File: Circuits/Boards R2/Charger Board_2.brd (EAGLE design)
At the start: 101.6 x 69.8 mm, 100 parts, among them CON1 ISP(2X3), CON10 HEADER_3X1, CON11 HEADER_3X1, CON12 HEADER_3X1, CON13 HEADER_4X1, CON14 HEADER_3X1, CON15 HEADER_3X1, CON16 HEADER_4X1, CON17 HEADER_3X1, CON18 HEADER_3X1, CON2 SCREWTERMINAL_1X2, CON3 HEADER_3X1, CON4 HEADER_3X1, CON5 HEADER_3X1, CON6 HEADER_3X1, CON7 HEADER_3X1, CON8 HEADER_3X1, CON9 HEADER_3X1, IC1 NCP1117DT33G, T1 NPN2N2222, T2 NPN2N2222, T3 SI4421DY, T4 MMSS8550-L, T5 MMSS8550-L, T6 MMSS8550-L, U1 ATMEGA324P, U2 ACS711, U3 JOYSTICKPTH, U4 MX25L25735E

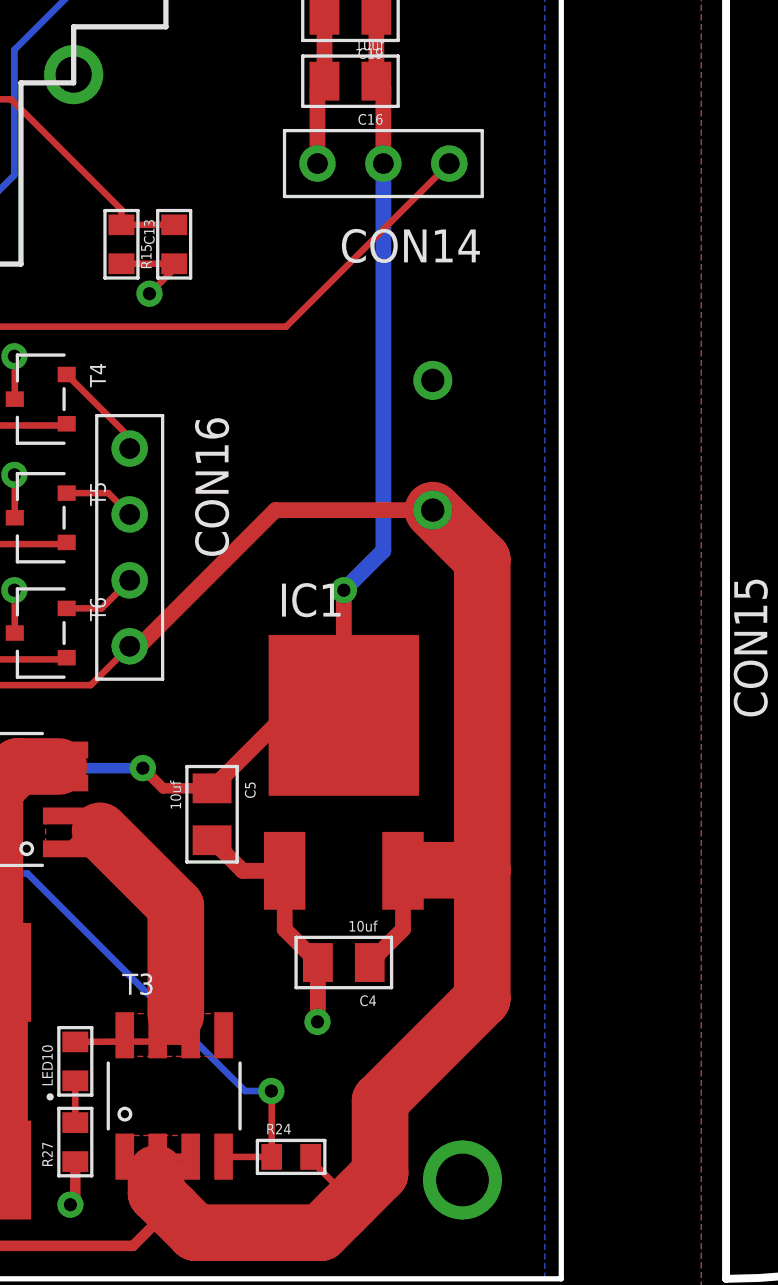
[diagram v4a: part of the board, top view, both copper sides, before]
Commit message: slight updates to part values to account for availibility
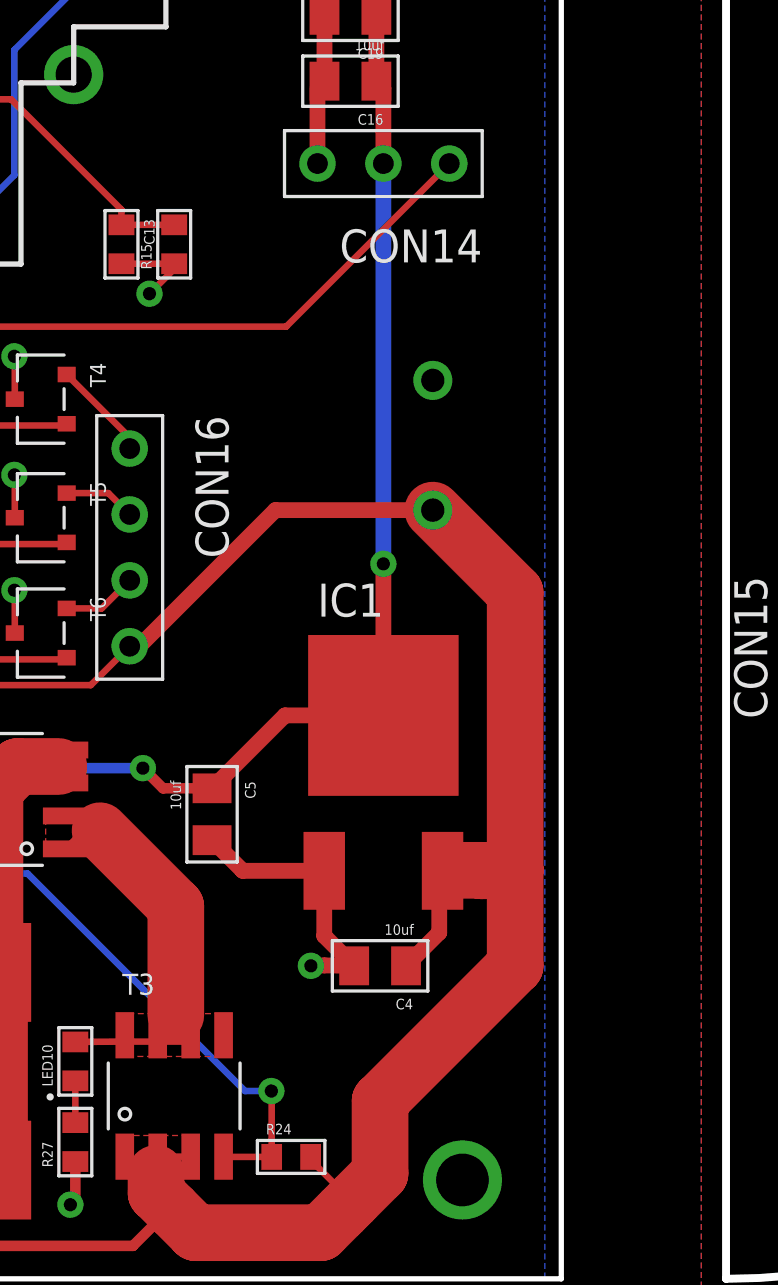
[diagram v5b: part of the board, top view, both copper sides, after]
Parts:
- R10, R11, R12, R13, R14, R25: value 18 -> 15
- moved IC1 1.52 mm to (63.0, 21.7)
- moved C4 1.40 mm to (62.9, 12.1)
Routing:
- net +5V: track 116.1 -> 117.1 mm
- net GND: track 70.6 -> 71.6 mm
- net +3V3: track 229.9 -> 230.8 mm
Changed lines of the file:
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@@
 <?xml version="1.0" encoding="utf-8"?>
 <!DOCTYPE eagle SYSTEM "eagle.dtd">
-<eagle version="6.3">
+<eagle version="6.2">
 <drawing>
 <settings>
@@
 </class>
 </classes>
-<designrules name="default">
+<designrules>
 <description language="en">&lt;b&gt;EAGLE Design Rules&lt;/b&gt;
 &lt;p&gt;
@@
 <element name="T1" library="Passive" package="SOT23" value="NPN2N2222" x="26.2255" y="54.6735" rot="R180"/>
 <element name="T2" library="Passive" package="SOT23" value="NPN2N2222" x="87.9475" y="21.9075" rot="R90"/>
-<element name="R10" library="Passive" package="0603" value="18" x="94.2975" y="15.5575" rot="R180"/>
-<element name="R11" library="Passive" package="0603" value="18" x="79.6925" y="10.795" rot="R270"/>
-<element name="R12" library="Passive" package="0603" value="18" x="93.345" y="35.8775" rot="R180"/>
-<element name="R13" library="Passive" package="0603" value="18" x="86.0425" y="43.4975" rot="R270"/>
-<element name="R14" library="Passive" package="0603" value="18" x="96.2025" y="26.67" rot="R180"/>
+<element name="R10" library="Passive" package="0603" value="15" x="94.2975" y="15.5575" rot="R180"/>
+<element name="R11" library="Passive" package="0603" value="15" x="79.6925" y="10.795" rot="R270"/>
+<element name="R12" library="Passive" package="0603" value="15" x="93.345" y="35.8775" rot="R180"/>
+<element name="R13" library="Passive" package="0603" value="15" x="86.0425" y="43.4975" rot="R270"/>
+<element name="R14" library="Passive" package="0603" value="15" x="96.2025" y="26.67" rot="R180"/>
 <element name="R16" library="Passive" package="0603" value="1k" x="83.82" y="22.86"/>
 <element name="LED2" library="Passive" package="5MM_LED_RA" value="IR" x="93.726" y="20.447" rot="R255"/>
@@
 <element name="CON11" library="Mechanical" package="3PINHEADER_.100&quot;" value="HEADER_3X1" x="34.29" y="8.001" rot="R90"/>
 <element name="CON12" library="Mechanical" package="3PINHEADER_.100&quot;" value="HEADER_3X1" x="36.83" y="8.001" rot="R90"/>
-<element name="IC1" library="PowerIC" package="DPAK" value="NCP1117DT33G" x="61.468" y="21.717"/>
-<element name="C4" library="Passive" package="0805" value="10uf" x="61.468" y="12.192" rot="R180"/>
+<element name="IC1" library="PowerIC" package="DPAK" value="NCP1117DT33G" x="62.992" y="21.717"/>
+<element name="C4" library="Passive" package="0805" value="10uf" x="62.865" y="12.065" rot="R180"/>
 <element name="C5" library="Passive" package="0805" value="10uf" x="56.388" y="17.907" rot="R270"/>
 <element name="T3" library="Passive" package="S0-8" value="SI4421DY" x="54.9275" y="7.0485"/>
@@
 <element name="C21" library="Passive" package="0603" value=".1uf" x="61.722" y="54.737" rot="R180"/>
 <element name="LED7" library="Passive" package="5MM_LED_RA" value="IR" x="89.66835" y="11.93165" rot="R225"/>
-<element name="R25" library="Passive" package="0603" value="18" x="86.36" y="8.5725" rot="R90"/>
+<element name="R25" library="Passive" package="0603" value="15" x="86.36" y="8.5725" rot="R90"/>
 <element name="H5" library="Mechanical" package="MOUNTINGHOLE" value="MOUNTINGHOLE" x="80.01" y="35.56"/>
 <element name="H6" library="Mechanical" package="MOUNTINGHOLE" value="MOUNTINGHOLE" x="80.01" y="15.24"/>
@@
 <vertex x="0" y="0"/>
 </polygon>
-<wire x1="59.188" y1="15.727" x2="57.568" y2="15.727" width="0.6096" layer="1"/>
+<wire x1="60.712" y1="15.727" x2="57.568" y2="15.727" width="0.6096" layer="1"/>
 <wire x1="57.568" y1="15.727" x2="56.388" y2="16.907" width="0.6096" layer="1"/>
-<wire x1="59.188" y1="15.727" x2="59.188" y2="13.472" width="0.6096" layer="1"/>
-<wire x1="59.188" y1="13.472" x2="60.468" y2="12.192" width="0.6096" layer="1"/>
+<wire x1="60.712" y1="15.727" x2="60.712" y2="13.218" width="0.6096" layer="1"/>
+<wire x1="60.712" y1="13.218" x2="61.865" y2="12.065" width="0.6096" layer="1"/>
 <wire x1="3.556" y1="20.816" x2="3.556" y2="22.364" width="0.254" layer="1"/>
 <wire x1="3.556" y1="20.816" x2="2.802" y2="20.82" width="0.254" layer="1"/>
@@
 <wire x1="24.13" y1="28.575" x2="23.876" y2="28.321" width="0.254" layer="1"/>
 <via x="23.876" y="28.321" extent="1-16" drill="0.508"/>
-<wire x1="60.468" y1="12.192" x2="60.468" y2="9.922" width="0.6096" layer="1"/>
-<wire x1="60.468" y1="9.922" x2="60.452" y2="9.906" width="0.6096" layer="1"/>
-<via x="60.452" y="9.906" extent="1-16" drill="0.508"/>
+<wire x1="61.865" y1="12.065" x2="60.722" y2="12.081" width="0.6096" layer="1"/>
+<wire x1="60.722" y1="12.081" x2="60.198" y2="12.065" width="0.6096" layer="1"/>
+<via x="60.198" y="12.065" extent="1-16" drill="0.508"/>
 <wire x1="18.38" y1="25.4" x2="16.891" y2="25.4" width="0.254" layer="1"/>
 <wire x1="16.891" y1="25.4" x2="16.764" y2="25.273" width="0.254" layer="1"/>
@@
 <contactref element="IC1" pad="3"/>
 <contactref element="C4" pad="1"/>
-<wire x1="63.748" y1="15.727" x2="63.748" y2="15.24" width="0.6096" layer="1"/>
-<wire x1="63.748" y1="15.24" x2="63.748" y2="13.472" width="0.6096" layer="1"/>
-<wire x1="63.748" y1="13.472" x2="62.468" y2="12.192" width="0.6096" layer="1"/>
+<wire x1="65.272" y1="15.727" x2="65.145" y2="15.24" width="0.6096" layer="1"/>
+<wire x1="65.145" y1="15.24" x2="65.145" y2="13.345" width="0.6096" layer="1"/>
+<wire x1="65.145" y1="13.345" x2="63.865" y2="12.065" width="0.6096" layer="1"/>
 <polygon width="0.254" layer="1" thermals="no">
 <vertex x="55.8165" y="3.8735"/>
@@
 <contactref element="LED1" pad="2"/>
 <contactref element="CON13" pad="1"/>
-<wire x1="66.781" y1="15.727" x2="66.802" y2="15.748" width="2.1844" layer="1"/>
+<wire x1="66.781" y1="15.727" x2="68.072" y2="15.748" width="2.1844" layer="1"/>
 <wire x1="61.4045" y1="2.6035" x2="60.579" y2="1.778" width="2.1844" layer="1"/>
 <wire x1="60.579" y1="1.778" x2="55.753" y2="1.778" width="2.1844" layer="1"/>
@@
 <wire x1="53.975" y1="4.391" x2="53.975" y2="4.191" width="0.254" layer="1"/>
 <wire x1="61.4045" y1="3.4805" x2="61.4045" y2="2.6035" width="0.254" layer="1"/>
-<wire x1="66.802" y1="15.748" x2="66.802" y2="10.795" width="2.1844" layer="1"/>
-<wire x1="66.802" y1="10.795" x2="62.865" y2="6.858" width="2.1844" layer="1"/>
+<wire x1="68.072" y1="15.748" x2="68.072" y2="12.065" width="2.1844" layer="1"/>
+<wire x1="68.072" y1="12.065" x2="62.865" y2="6.858" width="2.1844" layer="1"/>
 <wire x1="62.865" y1="6.858" x2="62.865" y2="4.064" width="2.1844" layer="1"/>
 <wire x1="62.865" y1="4.064" x2="61.7855" y2="2.9845" width="2.1844" layer="1"/>
 <wire x1="61.7855" y1="2.9845" x2="61.4045" y2="2.6035" width="2.1844" layer="1"/>
-<wire x1="64.897" y1="29.631" x2="66.802" y2="27.726" width="2.1844" layer="1"/>
-<wire x1="66.802" y1="27.726" x2="66.802" y2="15.748" width="2.1844" layer="1"/>
+<wire x1="64.897" y1="29.631" x2="68.072" y2="26.456" width="2.1844" layer="1"/>
+<wire x1="68.072" y1="26.456" x2="68.072" y2="15.748" width="2.1844" layer="1"/>
 <wire x1="66.781" y1="15.727" x2="66.76" y2="15.748" width="2.1844" layer="1"/>
-<wire x1="66.76" y1="15.748" x2="64.389" y2="15.748" width="2.1844" layer="1"/>
-<wire x1="64.389" y1="15.748" x2="63.881" y2="15.24" width="0.2032" layer="1"/>
-<wire x1="63.881" y1="15.24" x2="63.748" y2="15.24" width="0.2032" layer="1"/>
+<wire x1="66.76" y1="15.748" x2="65.913" y2="15.748" width="2.1844" layer="1"/>
+<wire x1="65.913" y1="15.748" x2="65.532" y2="15.367" width="0.2032" layer="1"/>
+<wire x1="65.532" y1="15.367" x2="65.145" y2="15.24" width="0.2032" layer="1"/>
 <contactref element="R24" pad="2"/>
 <contactref element="CON16" pad="4"/>
@@
 <contactref element="C5" pad="1"/>
 <wire x1="56.388" y1="18.907" x2="59.198" y2="21.717" width="0.6096" layer="1"/>
-<wire x1="59.198" y1="21.717" x2="61.468" y2="21.717" width="0.6096" layer="1"/>
+<wire x1="59.198" y1="21.717" x2="62.992" y2="21.717" width="0.6096" layer="1"/>
 <wire x1="18.38" y1="26.2" x2="24.13" y2="26.2" width="0.254" layer="1"/>
 <wire x1="24.13" y1="26.2" x2="27.051" y2="26.2" width="0.254" layer="1"/>
@@
 <wire x1="46.609" y1="40.386" x2="46.482" y2="40.259" width="0.254" layer="16"/>
 <wire x1="46.482" y1="40.259" x2="46.482" y2="19.685" width="0.254" layer="16"/>
-<wire x1="62.992" y1="42.9895" x2="62.992" y2="28.067" width="0.6096" layer="16"/>
-<wire x1="62.992" y1="28.067" x2="61.468" y2="26.543" width="0.6096" layer="16"/>
-<via x="61.468" y="26.543" extent="1-16" drill="0.508"/>
-<wire x1="61.468" y1="26.543" x2="61.468" y2="21.717" width="0.6096" layer="1"/>
+<wire x1="62.992" y1="42.9895" x2="62.992" y2="27.559" width="0.6096" layer="16"/>
+<via x="62.992" y="27.559" extent="1-16" drill="0.508"/>
+<wire x1="62.992" y1="27.559" x2="62.992" y2="21.717" width="0.6096" layer="1"/>
 <wire x1="62.992" y1="42.9895" x2="62.992" y2="45.8945" width="0.6096" layer="1"/>
 <wire x1="62.992" y1="45.8945" x2="62.722" y2="46.1645" width="0.6096" layer="1"/>

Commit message: added gerbers for production
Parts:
- moved CON15 4.45 mm to (75.9, 25.4)
- moved H5 4.45 mm to (75.6, 35.6)
- moved H6 4.45 mm to (75.6, 15.2)
- moved LED3 4.45 mm to (76.7, 7.87)
- moved LED4 4.45 mm to (85.2, 38.9)
- moved LED7 4.45 mm to (85.2, 11.9)
- moved R13 4.45 mm to (81.6, 43.5)
- moved R14 4.45 mm to (91.8, 26.7)
- moved T2 4.45 mm to (83.5, 21.9)
- moved C12 4.44 mm to (81.3, 27.0)
- moved C2 4.44 mm to (83.2, 27.0)
- moved C6 4.44 mm to (80.3, 31.1)
- moved C7 4.44 mm to (85.1, 27.0)
- moved C8 4.44 mm to (80.3, 33.7)
- moved C9 4.44 mm to (79.4, 27.0)
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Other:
- board size 101.6 x 69.8 mm -> 97.2 x 69.8 mm
- board text added: "+"
- board text added: "-"
- board text added: "12/10/12"
- board text added: "Cal Poly Robotics Club"
- board text added: "I2C"
- board text added: "IR TX"
- board text added: "Jeffrey D'Amelio"
- board text added: "LEDs"
- board text added: "UART 1"
- board text added: "UART 2"
- board text added: "s"
